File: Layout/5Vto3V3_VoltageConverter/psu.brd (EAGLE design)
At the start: 100 x 80 mm, 15 parts

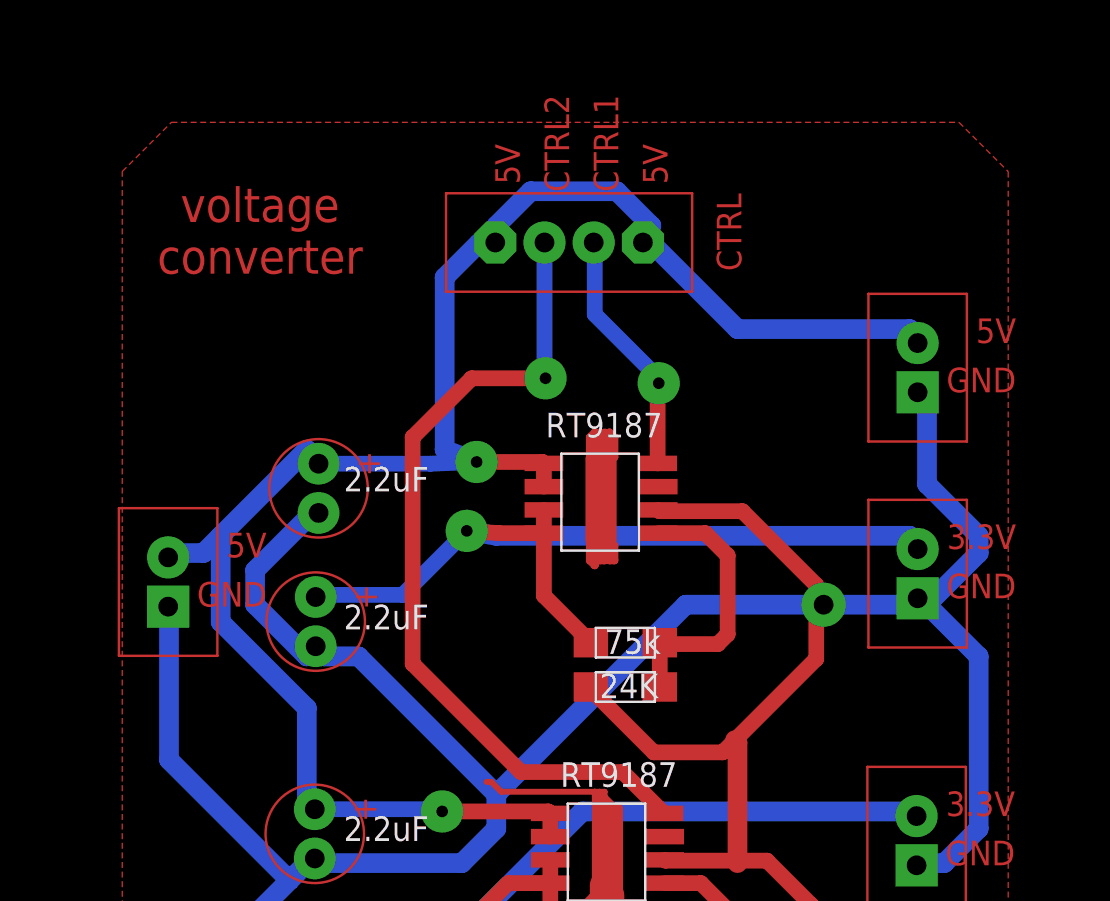
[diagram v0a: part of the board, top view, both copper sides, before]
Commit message: 添加3v3電壓轉換器usb接頭
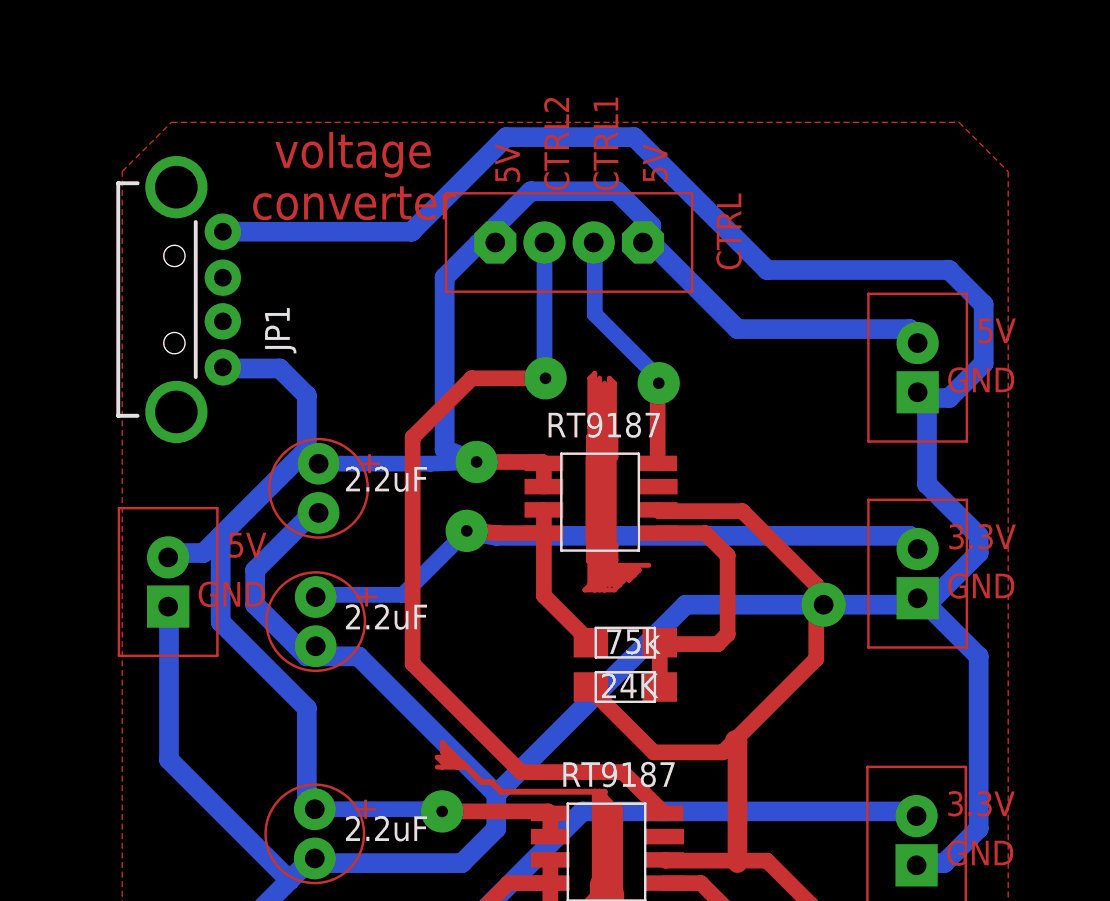
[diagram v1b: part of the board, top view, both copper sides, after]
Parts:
- added JP1: USB-A-H, SparkFun-Connectors:USB-A-H
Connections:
- net GND: now also JP1.GND
- net N$14: now also JP1.VBUS
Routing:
- net GND: track 182.8 -> 234.3 mm
- net N$25: track 0.00 -> 20.4 mm
- net N$11: track 9.42 -> 29.7 mm
- net N$24: track 10.9 -> 20.3 mm
- net N$14: track 94.6 -> 102.3 mm
